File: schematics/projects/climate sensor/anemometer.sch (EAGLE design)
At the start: 2 parts, among them U1 HALL_SENSOR, U2 HALL_SENSOR

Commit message: Continue prepare schematics to create board
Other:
- moved on the sheet: U1, U2
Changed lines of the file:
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@@
 </classes>
 <parts>
+<part name="U2" library="my_devices" deviceset="HALL_SENSOR" device=""/>
 <part name="U1" library="my_devices" deviceset="HALL_SENSOR" device=""/>
-<part name="U2" library="my_devices" deviceset="HALL_SENSOR" device=""/>
 <part name="GND1" library="supply1" library_urn="urn:adsk.eagle:library:371" deviceset="GND" device=""/>
 <part name="P+1" library="supply1" library_urn="urn:adsk.eagle:library:371" deviceset="+5V" device=""/>
@@
 </plain>
 <instances>
-<instance part="U1" gate="G$1" x="17.78" y="0" smashed="yes">
+<instance part="U2" gate="G$1" x="17.78" y="0" smashed="yes">
 <attribute name="NAME" x="25.4" y="0" size="1.778" layer="94"/>
 <attribute name="VALUE" x="25.4" y="-2.54" size="1.778" layer="94"/>
 </instance>
-<instance part="U2" gate="G$1" x="-22.86" y="0" smashed="yes">
+<instance part="U1" gate="G$1" x="-22.86" y="0" smashed="yes">
 <attribute name="NAME" x="-15.24" y="0" size="1.778" layer="94"/>
 <attribute name="VALUE" x="-15.24" y="-2.54" size="1.778" layer="94"/>
@@
 <net name="VCC" class="0">
 <segment>
+<pinref part="U1" gate="G$1" pin="VCC"/>
 <pinref part="U2" gate="G$1" pin="VCC"/>
-<pinref part="U1" gate="G$1" pin="VCC"/>
 <wire x1="-22.86" y1="7.62" x2="-5.08" y2="7.62" width="0.1524" layer="91"/>
 <pinref part="P+1" gate="1" pin="+5V"/>
@@
 <net name="GND" class="0">
 <segment>
+<pinref part="U2" gate="G$1" pin="GND"/>
 <pinref part="U1" gate="G$1" pin="GND"/>
-<pinref part="U2" gate="G$1" pin="GND"/>
 <wire x1="17.78" y1="-7.62" x2="-2.54" y2="-7.62" width="0.1524" layer="91"/>
 <pinref part="GND1" gate="1" pin="GND"/>
@@
 </segment>
 </net>
-<net name="OUT_B" class="0">
+<net name="OUT_A" class="0">
 <segment>
-<pinref part="U2" gate="G$1" pin="OUT"/>
+<pinref part="U1" gate="G$1" pin="OUT"/>
 <wire x1="-30.48" y1="0" x2="-30.48" y2="25.4" width="0.1524" layer="91"/>
 <label x="-30.48" y="22.86" size="1.778" layer="95"/>
 </segment>
 </net>
-<net name="OUT_A" class="0">
+<net name="OUT_B" class="0">
 <segment>
-<pinref part="U1" gate="G$1" pin="OUT"/>
+<pinref part="U2" gate="G$1" pin="OUT"/>
 <wire x1="10.16" y1="0" x2="10.16" y2="25.4" width="0.1524" layer="91"/>
 <label x="10.16" y="22.86" size="1.778" layer="95"/>

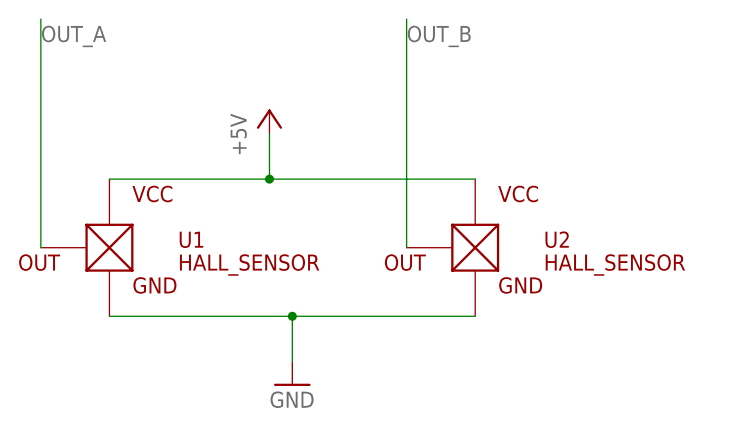
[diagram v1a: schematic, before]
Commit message: Changed some nomanals during making order
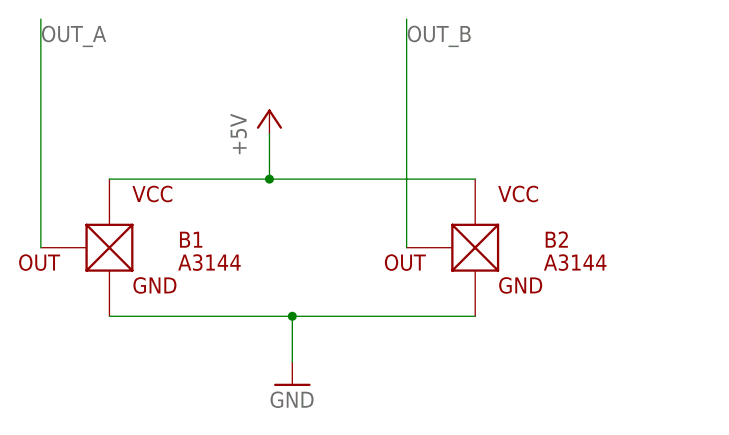
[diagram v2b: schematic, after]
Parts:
- B1, B2: value HALL_SENSOR -> A3144
- renumbered U1 to B1, U2 to B2
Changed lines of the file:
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@@
 </classes>
 <parts>
-<part name="U2" library="my_devices" deviceset="HALL_SENSOR" device=""/>
-<part name="U1" library="my_devices" deviceset="HALL_SENSOR" device=""/>
+<part name="B2" library="my_devices" deviceset="HALL_SENSOR" device="" value="A3144"/>
+<part name="B1" library="my_devices" deviceset="HALL_SENSOR" device="" value="A3144"/>
 <part name="GND1" library="supply1" library_urn="urn:adsk.eagle:library:371" deviceset="GND" device=""/>
 <part name="P+1" library="supply1" library_urn="urn:adsk.eagle:library:371" deviceset="+5V" device=""/>
@@
 </plain>
 <instances>
-<instance part="U2" gate="G$1" x="17.78" y="0" smashed="yes">
+<instance part="B2" gate="G$1" x="17.78" y="0" smashed="yes">
 <attribute name="NAME" x="25.4" y="0" size="1.778" layer="94"/>
 <attribute name="VALUE" x="25.4" y="-2.54" size="1.778" layer="94"/>
 </instance>
-<instance part="U1" gate="G$1" x="-22.86" y="0" smashed="yes">
+<instance part="B1" gate="G$1" x="-22.86" y="0" smashed="yes">
 <attribute name="NAME" x="-15.24" y="0" size="1.778" layer="94"/>
 <attribute name="VALUE" x="-15.24" y="-2.54" size="1.778" layer="94"/>
@@
 <net name="VCC" class="0">
 <segment>
-<pinref part="U1" gate="G$1" pin="VCC"/>
-<pinref part="U2" gate="G$1" pin="VCC"/>
+<pinref part="B1" gate="G$1" pin="VCC"/>
+<pinref part="B2" gate="G$1" pin="VCC"/>
 <wire x1="-22.86" y1="7.62" x2="-5.08" y2="7.62" width="0.1524" layer="91"/>
 <pinref part="P+1" gate="1" pin="+5V"/>
@@
 <net name="GND" class="0">
 <segment>
-<pinref part="U2" gate="G$1" pin="GND"/>
-<pinref part="U1" gate="G$1" pin="GND"/>
+<pinref part="B2" gate="G$1" pin="GND"/>
+<pinref part="B1" gate="G$1" pin="GND"/>
 <wire x1="17.78" y1="-7.62" x2="-2.54" y2="-7.62" width="0.1524" layer="91"/>
 <pinref part="GND1" gate="1" pin="GND"/>
@@
 <net name="OUT_A" class="0">
 <segment>
-<pinref part="U1" gate="G$1" pin="OUT"/>
+<pinref part="B1" gate="G$1" pin="OUT"/>
 <wire x1="-30.48" y1="0" x2="-30.48" y2="25.4" width="0.1524" layer="91"/>
 <label x="-30.48" y="22.86" size="1.778" layer="95"/>
@@
 <net name="OUT_B" class="0">
 <segment>
-<pinref part="U2" gate="G$1" pin="OUT"/>
+<pinref part="B2" gate="G$1" pin="OUT"/>
 <wire x1="10.16" y1="0" x2="10.16" y2="25.4" width="0.1524" layer="91"/>
 <label x="10.16" y="22.86" size="1.778" layer="95"/>
